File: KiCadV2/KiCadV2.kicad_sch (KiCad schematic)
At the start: 40 parts, among them J1 USB_C_Receptacle_PowerOnly_6P, J2 Screw_Terminal_01x02, J3 Screw_Terminal_01x02, J4 Screw_Terminal_01x02, U1 MT3608, U2 74HC595

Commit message: idk
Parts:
- removed R7: 10k, Resistor_SMD:R_0603_1608Metric, symbol Device:R
- removed U10, U11, U6, U7: ~, Package_TO_SOT_SMD:SOT-363_SC-70-6, symbol 74xx:NC7SZ157P6X
- added C4: 100n, Capacitor_SMD:C_0603_1608Metric, symbol Device:C
- added R8: 10k, Resistor_SMD:R_0603_1608Metric, symbol Device:R
- added U6: 74LV08AT14-13, Package_SO:TSSOP-14_4.4x5mm_P0.65mm, symbol 74xx:74LV08AT14-13
- added U9: GT74LVC6G14TD, Package_SO:TSSOP-14_4.4x5mm_P0.65mm, symbol 74xx:74HC04
- A1: now left out of the parts list
- C1: LCSC (none) -> C12891
- C2: LCSC (none) -> C14663
- C3: LCSC (none) -> C23630
- D1: value D -> D_power; footprint Diode_SMD:D_SMA -> Diode_SMD:D_SOD-123; LCSC (none) -> C8598
- D2: renamed from D14; value D_Schottky -> D_5.1V
- D3: renamed from D2; value D -> D_logic; LCSC (none) -> C7502714
- D4: renamed from D3; value D -> D_logic; LCSC (none) -> C7502714
- D5: renamed from D4; value LED -> KT-0603W; LCSC (none) -> C2290
- D6: renamed from D5; value LED -> KT-0603W; LCSC (none) -> C2290
- J2: renamed from J4; now left out of the parts list
- J3: renamed from J2; now left out of the parts list
- J4: renamed from J3; now left out of the parts list
- L1: footprint Inductor_THT:L_Axial_L5.3mm_D2.2mm_P2.54mm_Vertical_Vishay_IM-1 -> (none); LCSC (none) -> C15029
- R1: LCSC (none) -> C25804
- R10, R9: value 12.25k -> 12k; LCSC (none) -> C22790
- R11, R12: value 250 -> 100; LCSC (none) -> C22775
- R13, R14: value 400 -> 390; LCSC (none) -> C23151
- R2: value 19k -> 18k; LCSC (none) -> C25810
- R3: LCSC (none) -> C21190
- R6: renamed from R8; LCSC (none) -> C25804
- R7: renamed from R6; LCSC (none) -> C25804
- U1: LCSC (none) -> C84817
- U2: LCSC (none) -> C5947
- U3, U4, U5: value ~ -> NC7SZ157P6X
- U7: renamed from U8; value ~ -> DAC082S085CISDX/NOPB
- U8: renamed from U9; value ~ -> MX3502S
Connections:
- net 0.2V: now also C4.2
- net EN1: now also U6.1 (A)
- net EN2: now also R8.1, U6.4 (A)
- net GND: now also C4.1, R8.2, U9.11, U9.13
- net PerCoil/EN: now also U6.3 (Y)
- net PerCoil1/EN: now also U6.6 (Y)
- net ~{OC1}: now also U6.2 (B), U9.1
- net ~{OC2}: now also U6.5 (B), U9.3
- net at R13.2: now also U9.2
- net at R14.2: now also U9.4
- new net: U6.7 (V-), U6.9 (V-)
- no-connect marks 15 -> 17
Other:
- note removed: "2 AND: EN1 && ~{OC1}"
- note removed: "2 Inv"
- moved on the sheet: R7

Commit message: schematic FINAL! (I hope)
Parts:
- removed C2: 100n, Capacitor_SMD:C_0603_1608Metric, symbol Device:C
- removed D5, D6: KT-0603W, LED_SMD:LED_0603_1608Metric, symbol Device:LED
- removed R10, R9: 12k, Resistor_SMD:R_0603_1608Metric, symbol Device:R
- removed R11, R12: 100, Resistor_SMD:R_0603_1608Metric, symbol Device:R
- removed R13, R14: 390, Resistor_SMD:R_0603_1608Metric, symbol Device:R
- removed U6: 74LV08AT14-13, Package_SO:TSSOP-14_4.4x5mm_P0.65mm, symbol 74xx:74LV08AT14-13
- removed U8: MX3502S, Package_SO:SOP-8_3.76x4.96mm_P1.27mm, symbol Comparator:MX3502
- removed U9: GT74LVC6G14TD, Package_SO:TSSOP-14_4.4x5mm_P0.65mm, symbol 74xx:74HC04
- added C1: 100uF, Capacitor_SMD:C_1206_3216Metric, symbol Device:C
- added C20, C21, C37, C38, C42: 2.2u, Capacitor_SMD:C_0603_1608Metric, symbol Device:C
- added C31, C32, C33, C34, C35, C36, C39, C40, C41: 100n, Capacitor_SMD:C_0603_1608Metric, symbol Device:C
- added D2: D_Power_Big, Diode_SMD:D_SMC, symbol Device:D_Schottky
- added R6: 1k, Resistor_SMD:R_0603_1608Metric, symbol Device:R
- added TP1: TestPoint, TestPoint:TestPoint_Pad_D2.5mm, symbol Connector:TestPoint
- added U14, U38: 74LV08AT14-13, Package_SO:TSSOP-14_4.4x5mm_P0.65mm, symbol 74xx:74LV08AT14-13
- added U17, U18, U26, U5: MX3502S, Package_SO:SOP-8_3.76x4.96mm_P1.27mm, symbol Comparator:MX3502
- C3: value 2.2u -> 100n; LCSC C23630 -> C14663
- C4: value 100n -> 470p; LCSC C14663 -> C396711
- D3: renamed from D2; footprint Diode_SMD:D_SMA -> Diode_SMD:D_SMB; LCSC (none) -> C19077494
- L1: value L -> 10u; footprint (none) -> Inductor_SMD:10uH C15029
- R7: value 10k -> 9.1k; LCSC C25804 -> C23260
- R8: value 10k -> 5.1k; LCSC C25804 -> C23186
- renumbered C1 to C2, D3 to D4, D4 to D5, R5 to R2, R2 to R3, R3 to R4, R4 to R5, R6 to R9, U5 to U6
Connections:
- net +5V: now also C20.1, C21.1, C37.1, C38.1, C39.1, C40.1, C41.1, C42.1; no longer C3.2
- net 0.2V: no longer C4.2
- net EN1: no longer R7.1
- net EN2: no longer R8.1
- net GND: now also C3.2, C4.2, C1.2, C20.2, C21.2, C31.2, C32.2, C33.2, C34.2, C35.2, C36.2, C37.2, C38.2, C39.2, C40.2, C41.2, C42.2, U14.7 (V-), U17.5 (V-), U18.5 (V-), U26.5 (V-), U38.7 (V-), U5.3 (+), U5.4 (-), U5.5 (V-); no longer C3.1, C4.1, R7.2, R8.2
- net VBUS: no longer D3.1 (K), J1.A9 (VBUS), J1.B9 (VBUS)
- net VCM: now also C3.1, R6.1
- net at U6.4 (Z), U7.8 (DIN): now also TP1.1
- new net: C32.1, U17.8 (V+)
- new net: C35.1, U14.14 (V+)
- new net: C36.1, U38.14 (V+)
- new net: C31.1, U5.8 (V+)
- new net: R6.2, R7.1, U5.1 (+)
- new net: D2.2 (A), J1.A9 (VBUS), J1.B9 (VBUS)
- new net: C34.1, U26.8 (V+)
- new net: C33.1, U18.8 (V+)
- new net Vdrive: C1.1, D2.1 (K), D3.1 (K)
- new net Vsq: R7.2, R8.2, U5.7
- new net Vtri: C4.1, R8.1, U5.2 (-)
- no-connect marks 17 -> 16
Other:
- sheet PerCoil ports: added 0.2V, Vtri; removed OC_SENSE
- sheet PerCoil1 ports: added 0.2V, Vtri; removed OC_SENSE
- note added: "12V Boost for HIP4080 & Arduino Vin"
- note added: "AND Gates"
- note added: "Coil drive (literally everything else)"
- note added: "Connection interfaces"
- note added: "Multi-body IC's - Power supply & decoupling caps"
- note added: "OC Comparators"
- note added: "PWM 1MHz Triangle wave generator"
- note added: "PWM Comparators"
- note added: "Shared references"
- note added: "State selection shift register"
- note added: "USB-C Power Input"
- note removed: "EN1 forces EN to GND if low. If high, EN = OC detection"
- note removed: "EN2 forces EN to GND if low. If high, EN = OC detection"
- note removed: "Over-current (OC) detection"
- note removed: "State selection"
- moved on the sheet: A1, C2, D1, D3, D4, D5, J1, J2, J3, J4, L1, R1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

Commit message: PCB Almost done with one coil!!
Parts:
- A1: footprint Module:Arduino_UNO_R3 -> Module:Arduino_UNO_R3_ConnOnly
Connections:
- net +5V: now also C31.1, C32.1, C33.1, C34.1, C35.1, C36.1, U14.14 (V+), U17.8 (V+), U18.8 (V+), U26.8 (V+), U38.14 (V+), U5.8 (V+)
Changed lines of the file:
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@@
 	)
 	(junction
-		(at 113.03 163.83)
-		(diameter 0)
-		(color 0 0 0 0)
-	)
-	(junction
 		(at 46.99 55.88)
 		(diameter 0)
@@
 	)
 	(junction
+		(at 80.01 166.37)
+		(diameter 0)
+		(color 0 0 0 0)
+	)
+	(junction
+		(at 55.88 166.37)
+		(diameter 0)
+		(color 0 0 0 0)
+	)
+	(junction
 		(at 54.61 27.94)
 		(diameter 0)
@@
 	)
 	(junction
-		(at 55.88 163.83)
+		(at 50.8 105.41)
 		(diameter 0)
 		(color 0 0 0 0)
 	)
 	(junction
-		(at 50.8 105.41)
+		(at 90.17 166.37)
 		(diameter 0)
 		(color 0 0 0 0)
 	)
 	(junction
-		(at 68.58 173.99)
+		(at 113.03 166.37)
 		(diameter 0)
 		(color 0 0 0 0)
 	)
 	(junction
-		(at 90.17 163.83)
+		(at 68.58 173.99)
 		(diameter 0)
 		(color 0 0 0 0)
@@
 	)
 	(junction
+		(at 68.58 166.37)
+		(diameter 0)
+		(color 0 0 0 0)
+	)
+	(junction
 		(at 22.86 78.74)
 		(diameter 0)
@@
 	)
 	(junction
+		(at 127 166.37)
+		(diameter 0)
+		(color 0 0 0 0)
+	)
+	(junction
 		(at 80.01 173.99)
 		(diameter 0)
@@
 	)
 	(junction
+		(at 33.02 166.37)
+		(diameter 0)
+		(color 0 0 0 0)
+	)
+	(junction
 		(at 50.8 78.74)
 		(diameter 0)
@@
 	)
 	(junction
+		(at 44.45 166.37)
+		(diameter 0)
+		(color 0 0 0 0)
+	)
+	(junction
+		(at 104.14 166.37)
+		(diameter 0)
+		(color 0 0 0 0)
+	)
+	(junction
 		(at 59.69 78.74)
 		(diameter 0)
@@
 	(wire
 		(pts
-			(xy 21.59 163.83) (xy 55.88 163.83)
-		)
-		(stroke
-			(width 0)
-			(type default)
-		)
-	)
-	(wire
-		(pts
 			(xy 195.58 20.32) (xy 195.58 21.59)
 		)
@@
 	(wire
 		(pts
-			(xy 55.88 163.83) (xy 90.17 163.83)
+			(xy 55.88 166.37) (xy 68.58 166.37)
 		)
 		(stroke
@@
 	(wire
 		(pts
-			(xy 90.17 163.83) (xy 90.17 166.37)
+			(xy 113.03 166.37) (xy 127 166.37)
 		)
 		(stroke
@@
 	(wire
 		(pts
-			(xy 113.03 163.83) (xy 113.03 166.37)
-		)
-		(stroke
-			(width 0)
-			(type default)
-		)
-	)
-	(wire
-		(pts
 			(xy 81.28 35.56) (xy 81.28 36.83)
 		)
@@
 	(wire
 		(pts
-			(xy 240.03 147.32) (xy 240.03 151.13)
+			(xy 127 166.37) (xy 135.89 166.37)
 		)
 		(stroke
@@
 	(wire
 		(pts
-			(xy 168.91 34.29) (xy 168.91 39.37)
+			(xy 240.03 147.32) (xy 240.03 151.13)
 		)
 		(stroke
@@
 	(wire
 		(pts
-			(xy 124.46 110.49) (xy 127 110.49)
+			(xy 168.91 34.29) (xy 168.91 39.37)
 		)
 		(stroke
@@
 	(wire
 		(pts
-			(xy 127 173.99) (xy 113.03 173.99)
+			(xy 21.59 166.37) (xy 33.02 166.37)
 		)
 		(stroke
@@
 	(wire
 		(pts
-			(xy 105.41 97.79) (xy 109.22 97.79)
+			(xy 124.46 110.49) (xy 127 110.49)
 		)
 		(stroke
@@
 	(wire
 		(pts
-			(xy 45.72 40.64) (xy 48.26 40.64)
+			(xy 127 173.99) (xy 113.03 173.99)
 		)
 		(stroke
@@
 	(wire
 		(pts
-			(xy 38.1 78.74) (xy 41.91 78.74)
+			(xy 105.41 97.79) (xy 109.22 97.79)
 		)
 		(stroke
@@
 	(wire
 		(pts
-			(xy 54.61 27.94) (xy 59.69 27.94)
+			(xy 45.72 40.64) (xy 48.26 40.64)
 		)
 		(stroke
@@
 	(wire
 		(pts
-			(xy 205.74 62.23) (xy 215.9 62.23)
+			(xy 38.1 78.74) (xy 41.91 78.74)
 		)
 		(stroke
@@
 	(wire
 		(pts
-			(xy 257.81 73.66) (xy 260.35 73.66)
+			(xy 54.61 27.94) (xy 59.69 27.94)
 		)
 		(stroke
@@
 	(wire
 		(pts
-			(xy 34.29 101.6) (xy 34.29 105.41)
+			(xy 205.74 62.23) (xy 215.9 62.23)
 		)
 		(stroke
@@
 	(wire
 		(pts
-			(xy 48.26 55.88) (xy 46.99 55.88)
+			(xy 33.02 166.37) (xy 44.45 166.37)
 		)
 		(stroke
@@
 	(wire
 		(pts
-			(xy 90.17 173.99) (xy 80.01 173.99)
+			(xy 257.81 73.66) (xy 260.35 73.66)
 		)
 		(stroke
@@
 	(wire
 		(pts
-			(xy 45.72 50.8) (xy 45.72 55.88)
+			(xy 34.29 101.6) (xy 34.29 105.41)
 		)
 		(stroke
@@
 	(wire
 		(pts
-			(xy 113.03 163.83) (xy 135.89 163.83)
+			(xy 48.26 55.88) (xy 46.99 55.88)
 		)
 		(stroke
@@
 	(wire
 		(pts
-			(xy 41.91 91.44) (xy 41.91 78.74)
+			(xy 90.17 173.99) (xy 80.01 173.99)
 		)
 		(stroke
@@
 	(wire
 		(pts
-			(xy 31.75 133.35) (xy 34.29 133.35)
+			(xy 45.72 50.8) (xy 45.72 55.88)
 		)
 		(stroke
@@
 	(wire
 		(pts
-			(xy 184.15 46.99) (xy 187.96 46.99)
+			(xy 41.91 91.44) (xy 41.91 78.74)
 		)
 		(stroke
@@
 	(wire
 		(pts
-			(xy 86.36 132.08) (xy 86.36 129.54)
+			(xy 31.75 133.35) (xy 34.29 133.35)
 		)
 		(stroke
@@
 	(wire
 		(pts
-			(xy 135.89 163.83) (xy 135.89 166.37)
+			(xy 184.15 46.99) (xy 187.96 46.99)
 		)
 		(stroke
@@
 	(wire
 		(pts
-			(xy 55.88 163.83) (xy 55.88 166.37)
+			(xy 86.36 132.08) (xy 86.36 129.54)
 		)
 		(stroke
@@
 	(wire
 		(pts
+			(xy 104.14 166.37) (xy 113.03 166.37)
+		)
+		(stroke
+			(width 0)
+			(type default)
+		)
+	)
+	(wire
+		(pts
 			(xy 104.14 173.99) (xy 90.17 173.99)
 		)
@@
 	(wire
 		(pts
+			(xy 68.58 166.37) (xy 80.01 166.37)
+		)
+		(stroke
+			(width 0)
+			(type default)
+		)
+	)
+	(wire
+		(pts
 			(xy 127 120.65) (xy 127 123.19)
 		)
@@
 	(wire
 		(pts
-			(xy 90.17 163.83) (xy 113.03 163.83)
+			(xy 127 173.99) (xy 135.89 173.99)
 		)
 		(stroke
@@
 	(wire
 		(pts
-			(xy 135.89 173.99) (xy 127 173.99)
+			(xy 90.17 166.37) (xy 104.14 166.37)
+		)
+		(stroke
+			(width 0)
+			(type default)
+		)
+	)
+	(wire
+		(pts
+			(xy 80.01 166.37) (xy 90.17 166.37)
+		)
+		(stroke
+			(width 0)
+			(type default)
+		)
+	)
+	(wire
+		(pts
+			(xy 44.45 166.37) (xy 55.88 166.37)
 		)
 		(stroke
@@
 	(label "Vtri"
 		(at 113.03 120.65 0)
+		(fields_autoplaced yes)
 		(effects
 			(font
@@
 			(justify left bottom)
 		)
+		(property "Netclass" "HF"
+			(at 113.03 121.92 0)
+			(effects
+				(font
+					(size 1.27 1.27)
+					(italic yes)
+				)
+				(justify left)
+			)
+		)
 	)
 	(label "C2"
@@
 	(label "PWM5"
 		(at 201.93 41.91 180)
+		(fields_autoplaced yes)
 		(effects
 			(font
@@
 			(justify right bottom)
 		)
+		(property "Netclass" "HF"
+			(at 201.93 43.18 0)
+			(effects
+				(font
+					(size 1.27 1.27)
+					(italic yes)
+				)
+				(justify right)
+			)
+		)
 	)
 	(label "C1"
@@
 	(label "Vsq"
 		(at 127 97.79 0)
+		(fields_autoplaced yes)
 		(effects
 			(font
@@
 			(justify left bottom)
 		)
+		(property "Netclass" "HF"
+			(at 127 99.06 0)
+			(effects
+				(font
+					(size 1.27 1.27)
+					(italic yes)
+				)
+				(justify left)
+			)
+		)
 	)
 	(label "D3"
@@
 	(symbol
 		(lib_id "power:+5V")
-		(at 21.59 163.83 0)
+		(at 21.59 166.37 0)
 		(unit 1)
 		(exclude_from_sim no)
@@
 		(fields_autoplaced yes)
 		(property "Reference" "#PWR0104"
-			(at 21.59 167.64 0)
+			(at 21.59 170.18 0)
 			(effects
 				(font
@@
 		)
 		(property "Value" "+5V"
-			(at 21.59 158.75 0)
+			(at 21.59 161.29 0)
 			(effects
 				(font
@@
 		)
 		(property "Footprint" ""
-			(at 21.59 163.83 0)
+			(at 21.59 166.37 0)
 			(effects
 				(font
@@
 		)
 		(property "Datasheet" ""
-			(at 21.59 163.83 0)
+			(at 21.59 166.37 0)
 			(effects
 				(font
@@
 		)
 		(property "Description" "Power symbol creates a global label with name \"+5V\""
-			(at 21.59 163.83 0)
+			(at 21.59 166.37 0)
 			(effects
 				(font
@@
 			)
 		)
-		(property "Footprint" "Module:Arduino_UNO_R3"
+		(property "Footprint" "Module:Arduino_UNO_R3_ConnOnly"
 			(at 260.35 45.72 0)
 			(effects

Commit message: saving here before i try making PerCoilFlipped on schematic
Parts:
- removed C20, C21, C37, C38: 2.2u, Capacitor_SMD:C_0603_1608Metric, symbol Device:C
- removed D4, D5: D_logic, Diode_SMD:D_SMA, symbol Device:D
- removed R9: 10k, Resistor_SMD:R_0603_1608Metric, symbol Device:R
- added U16: NC7SZ157P6X, Package_TO_SOT_SMD:SOT-363_SC-70-6, symbol 74xx:NC7SZ157P6X
- A1: footprint Module:Arduino_UNO_R3_ConnOnly -> Module:Arduino_UNO_R3_ConnOnly_Coil_Driver
- U7: footprint Package_SON:WSON-10-1EP_3x3mm_P0.5mm_EP1.6x2mm -> WSON-10-1_3x3mm_P0.5mm_1.6x2mm
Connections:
- net +5V: now also U16.1 (I1), U16.5 (Vcc)
- net B1: now also U16.3 (I0)
- net C1: now also U16.6 (S)
- net GND: now also U16.2 (GND)
- net VBUS: now also D2.2 (A), J1.A9 (VBUS), J1.B9 (VBUS)
- net at U6.6 (S): now also U16.4 (Z)
- no-connect marks 16 -> 17
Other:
- note added: "B1 || C1"

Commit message: Fixed schematic after annotation fuck up
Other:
- sheet VoltageReferences: file untitled.kicad_sch -> VoltageReferences.kicad_sch
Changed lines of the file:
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@@
 			)
 		)
-		(property "Sheetfile" "untitled.kicad_sch"
+		(property "Sheetfile" "VoltageReferences.kicad_sch"
 			(at 19.05 140.2846 0)
 			(effects

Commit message: PCB - Right side coil done
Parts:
- removed J2: Screw_Terminal_01x02, Connector_PinHeader_2.54mm:PinHeader_2x01_P2.54mm_Vertical, symbol Connector:Screw_Terminal_01x02
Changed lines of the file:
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@@
-	)
-	(symbol
-		(lib_id "power:VBUS")
-		(at 250.19 102.87 90)
-		(unit 1)
-		(exclude_from_sim no)
-		(in_bom yes)
-		(on_board yes)
-		(dnp no)
-		(fields_autoplaced yes)
-		(property "Reference" "#PWR022"
-			(at 254 102.87 0)
-			(effects
-				(font
-					(size 1.27 1.27)
-				)
-				(hide yes)
-			)
-		)
-		(property "Value" "VBUS"
-			(at 246.38 102.8699 90)
-			(effects
-				(font
-					(size 1.27 1.27)
-				)
-				(justify left)
-			)
-		)
-		(property "Footprint" ""
-			(at 250.19 102.87 0)
-			(effects
-				(font
-					(size 1.27 1.27)
-				)
-				(hide yes)
-			)
-		)
-		(property "Datasheet" ""
-			(at 250.19 102.87 0)
-			(effects
-				(font
-					(size 1.27 1.27)
-				)
-				(hide yes)
-			)
-		)
-		(property "Description" "Power symbol creates a global label with name \"VBUS\""
-			(at 250.19 102.87 0)
-			(effects
-				(font
-					(size 1.27 1.27)
-				)
-				(hide yes)
-			)
-		)
-		(pin "1"
-		)
-		(instances
-			(project ""
-				(path "/e7727714-8b02-4dc5-9ae4-9abf282a37e0"
-					(reference "#PWR022")
-					(unit 1)
-				)
-			)
-		)
 	)
 	(symbol
@@
 	(symbol
 		(lib_id "power:GND")
-		(at 250.19 105.41 270)
-		(unit 1)
-		(exclude_from_sim no)
-		(in_bom yes)
-		(on_board yes)
-		(dnp no)
-		(fields_autoplaced yes)
-		(property "Reference" "#PWR023"
-			(at 243.84 105.41 0)
-			(effects
-				(font
-					(size 1.27 1.27)
-				)
-				(hide yes)
-			)
-		)
-		(property "Value" "GND"
-			(at 246.38 105.4099 90)
-			(effects
-				(font
-					(size 1.27 1.27)
-				)
-				(justify right)
-			)
-		)
-		(property "Footprint" ""
-			(at 250.19 105.41 0)
-			(effects
-				(font
-					(size 1.27 1.27)
-				)
-				(hide yes)
-			)
-		)
-		(property "Datasheet" ""
-			(at 250.19 105.41 0)
-			(effects
-				(font
-					(size 1.27 1.27)
-				)
-				(hide yes)
-			)
-		)
-		(property "Description" "Power symbol creates a global label with name \"GND\" , ground"
-			(at 250.19 105.41 0)
-			(effects
-				(font
-					(size 1.27 1.27)
-				)
-				(hide yes)
-			)
-		)
-		(pin "1"
-		)
-		(instances
-			(project "KiCadV2"
-				(path "/e7727714-8b02-4dc5-9ae4-9abf282a37e0"
-					(reference "#PWR023")
-					(unit 1)
-				)
-			)
-		)
-	)
-	(symbol
-		(lib_id "power:GND")
 		(at 59.69 35.56 0)
 		(unit 1)
@@
 				)
 			)
-		)
-	)
-	(symbol
-		(lib_id "Connector:Screw_Terminal_01x02")
-		(at 255.27 102.87 0)
-		(unit 1)
-		(exclude_from_sim no)
-		(in_bom no)
-		(on_board yes)
-		(dnp no)
-		(fields_autoplaced yes)
-		(property "Reference" "J2"
-			(at 257.81 102.8699 0)
-			(effects
-				(font
-					(size 1.27 1.27)
-				)
-				(justify left)
-			)
-		)
-		(property "Value" "Screw_Terminal_01x02"
-			(at 257.81 105.4099 0)
-			(effects
-				(font
-					(size 1.27 1.27)
-				)
-				(justify left)
-			)
-		)
-		(property "Footprint" "Connector_PinHeader_2.54mm:PinHeader_2x01_P2.54mm_Vertical"
-			(at 255.27 102.87 0)
-			(effects
-				(font
-					(size 1.27 1.27)
-				)
-				(hide yes)
-			)
-		)
-		(property "Datasheet" "~"
-			(at 255.27 102.87 0)
-			(effects
-				(font
-					(size 1.27 1.27)
-				)
-				(hide yes)
-			)
-		)
-		(property "Description" "Generic screw terminal, single row, 01x02, script generated (kicad-library-utils/schlib/autogen/connector/)"
-			(at 255.27 102.87 0)
-			(effects
-				(font
-					(size 1.27 1.27)
-				)
-				(hide yes)
-			)
-		)
-		(pin "1"
-		)
-		(pin "2"
-		)
-		(instances
-			(project "KiCadV2"
-				(path "/e7727714-8b02-4dc5-9ae4-9abf282a37e0"
-					(reference "J2")
-					(unit 1)
-				)
-			)

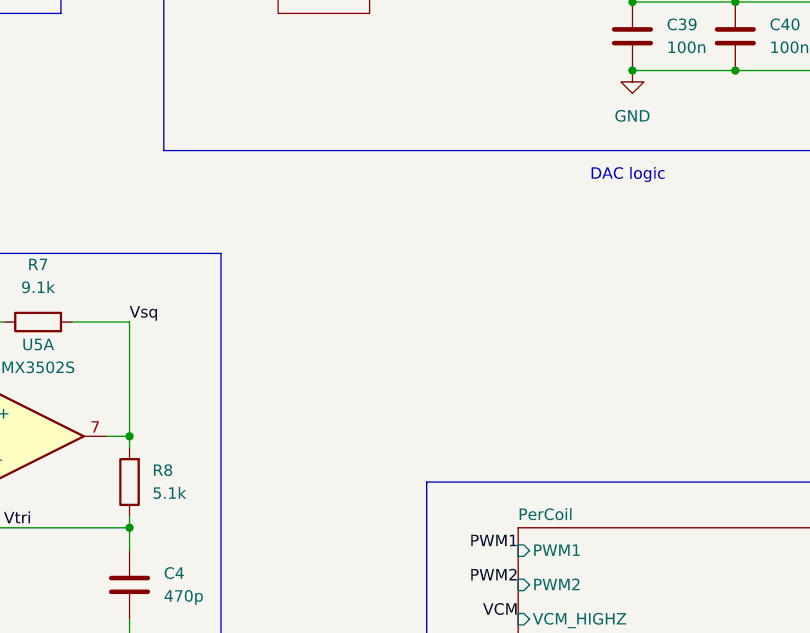
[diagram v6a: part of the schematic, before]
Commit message: Added LEDs to schematic & PCB
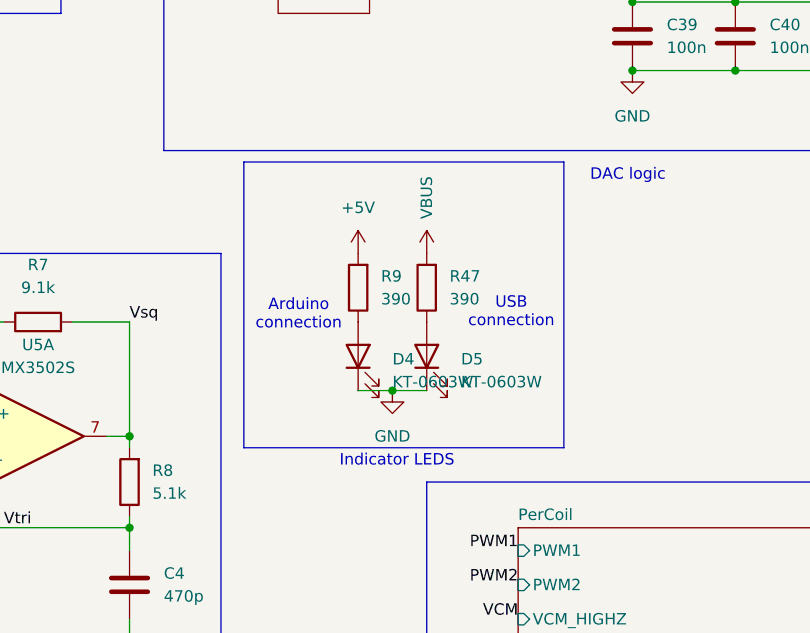
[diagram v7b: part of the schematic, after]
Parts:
- added D4, D5: KT-0603W, LED_SMD:LED_0603_1608Metric, symbol Device:LED
- added R47, R9: 390, Resistor_SMD:R_0603_1608Metric, symbol Device:R
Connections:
- net +5V: now also R9.2
- net GND: now also D4.1 (K), D5.1 (K)
- net VBUS: now also R47.2
- new net: D4.2 (A), R9.1
- new net: D5.2 (A), R47.1
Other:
- note added: "Arduino connection"
- note added: "Indicator LEDS"
- note added: "USB connection"
